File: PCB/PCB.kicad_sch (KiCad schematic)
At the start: 21 parts, among them J1 Conn_02x16_Row_Letter_Last_Sh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, U1 DRV8833PWP, U2 INA219AxDCN, U3 TPS22917DBV, U4 TPS22917DBV, U6 BQ24074RGT

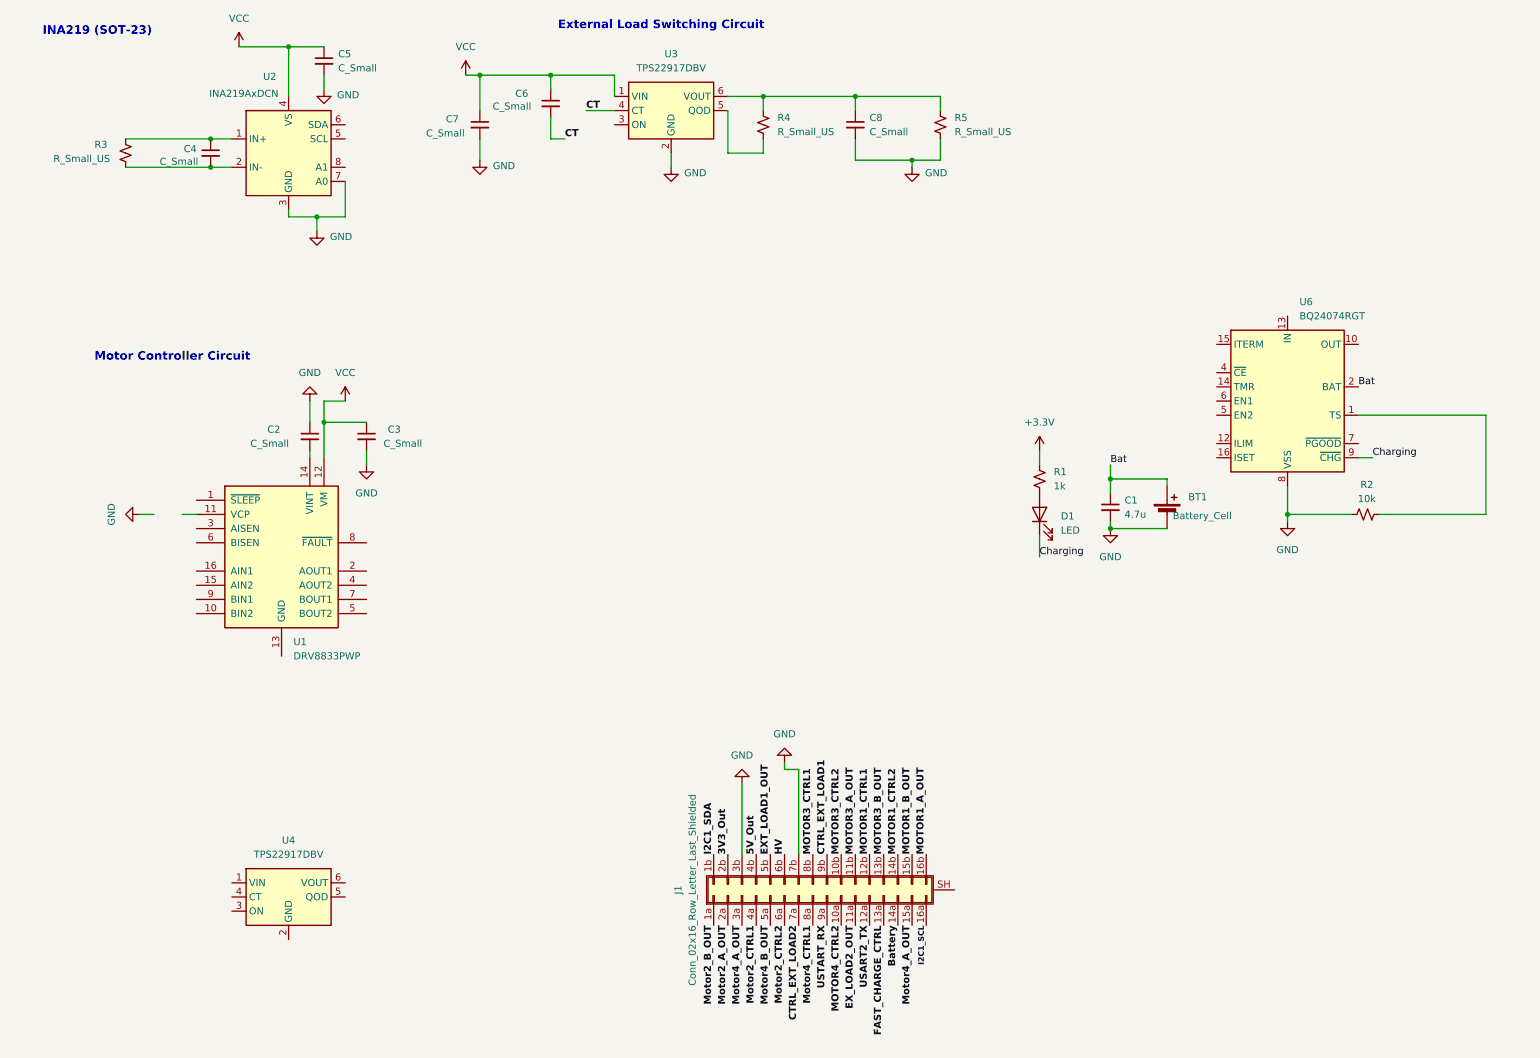
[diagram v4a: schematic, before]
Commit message: Changes to Layout
- An additional sheet was added
- ptxnya001's modules were placed into demarcated areas on her sheet
- ptxnya001's modules were given brief descriptions
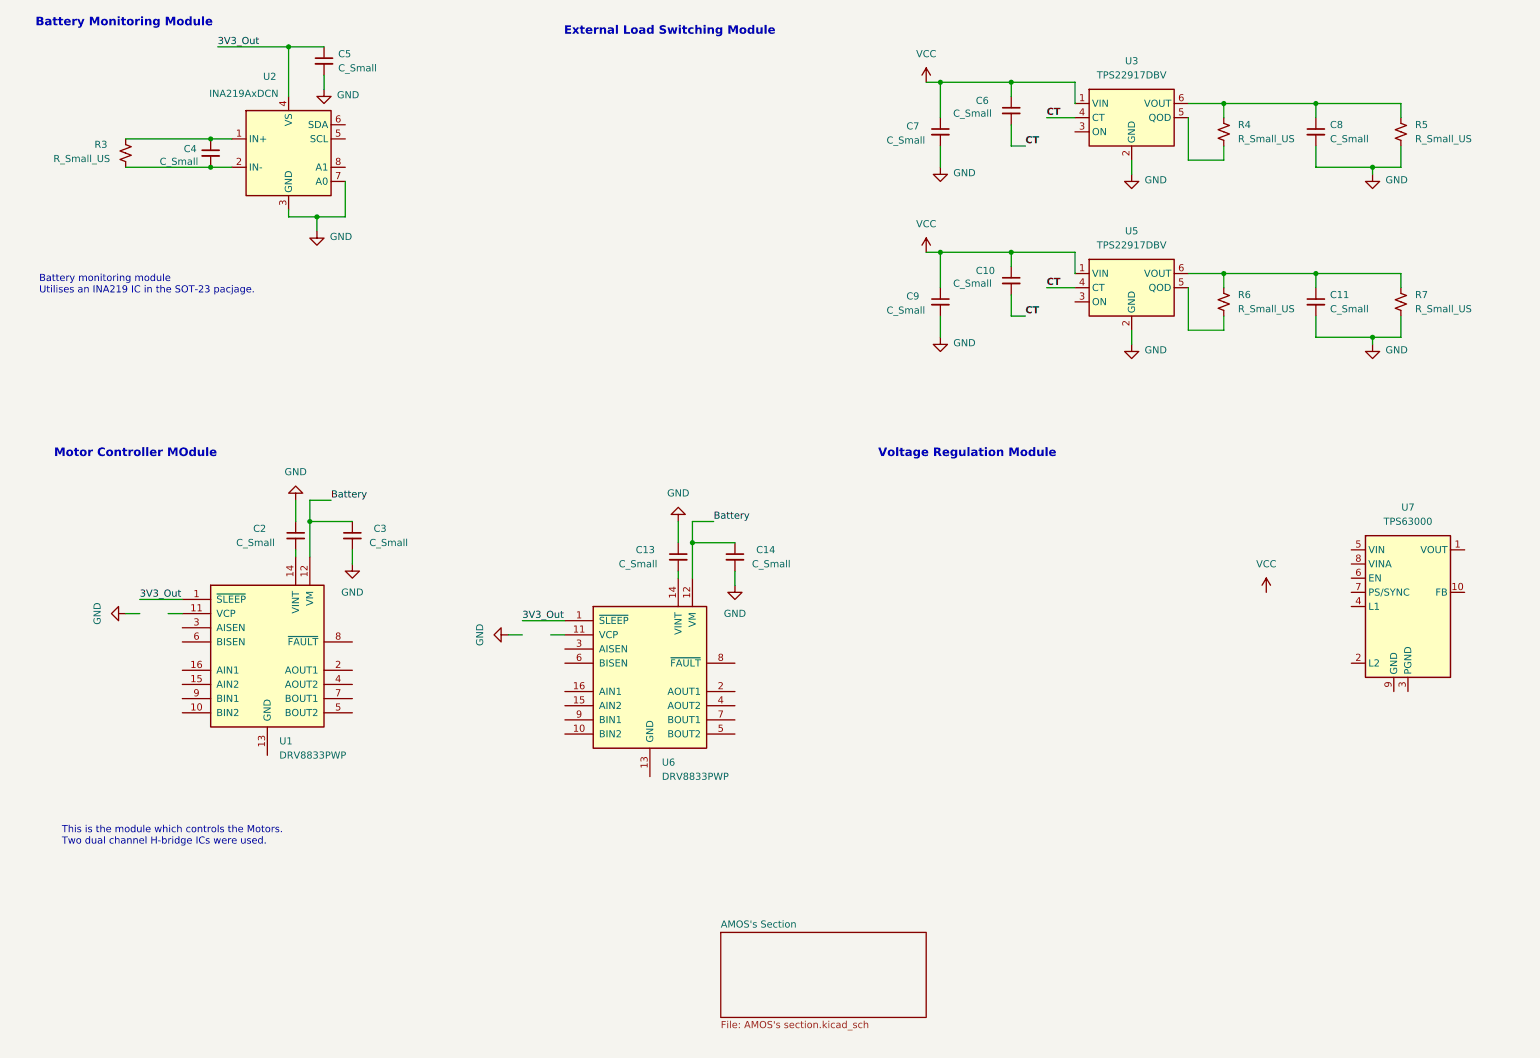
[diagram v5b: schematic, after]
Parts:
- removed BT1: Battery_Cell, symbol Device:Battery_Cell
- removed C1: 4.7u, symbol Device:C_Small
- removed D1: LED, symbol Device:LED
- removed J1: Conn_02x16_Row_Letter_Last_Shielded, symbol Connector_Generic_Shielded:Conn_02x16_Row_Letter_Last_Shielded
- removed R1: 1k, symbol Device:R_Small_US
- removed R2: 10k, symbol Device:R_Small_US
- removed U4: TPS22917DBV, Package_TO_SOT_SMD:SOT-23-6, symbol Power_Management:TPS22917DBV
- removed U6: BQ24074RGT, Package_DFN_QFN:VQFN-16-1EP_3x3mm_P0.5mm_EP1.6x1.6mm, symbol Battery_Management:BQ24074RGT
- added C10, C11, C13, C14, C9: C_Small, symbol Device:C_Small
- added R6, R7: R_Small_US, symbol Device:R_Small_US
- added U5: TPS22917DBV, Package_TO_SOT_SMD:SOT-23-6, symbol Power_Management:TPS22917DBV
- added U6: DRV8833PWP, Package_SO:HTSSOP-16-1EP_4.4x5mm_P0.65mm_EP3.4x5mm_Mask2.46x2.31mm_ThermalVias, symbol Driver_Motor:DRV8833PWP
- added U7: TPS63000, Package_SON:Texas_DRC0010J_ThermalVias, symbol Regulator_Switching:TPS63000
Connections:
- net 3V3_Out: now also C5.1, U1.1 (~{SLEEP}), U2.4 (VS), U6.1 (~{SLEEP})
- net Battery: now also C3.1, U1.12 (VM), C14.1, U6.12 (VM)
- net CT: now also C10.2, U5.4 (CT)
- net GND: now also C11.2, C13.1, C14.2, C9.2, R7.2, U5.2 (GND)
- net VCC: now also C10.1, C9.1, U5.1 (VIN); no longer C3.1, C5.1, U1.12 (VM), U2.4 (VS)
- new net: R6.2, U5.5 (QOD)
- new net: C11.1, R6.1, R7.1, U5.6 (VOUT)
- new net: U6.13 (GND), U6.17 (GND)
- new net: C13.2, U6.14 (VINT)
- new net: U7.11 (PGND), U7.3 (PGND)
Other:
- added sheet AMOS's Section (AMOS's section.kicad_sch)
- note added: "Battery Monitoring Module"
- note added: "Battery monitoring module Utilises an INA219 IC in the SOT-23 pacjage."
- note added: "External Load Switching Module"
- note added: "Motor Controller MOdule"
- note added: "This is the module which controls the Motors. Two dual channel H-bridge ICs were used."
- note added: "Voltage Regulation Module"
- note removed: "External Load Switching Circuit"
- note removed: "INA219 (SOT-23)"
- note removed: "Motor Controller Circuit"
- moved on the sheet: C2, C3, C6, C7, C8, R4, R5, U1, U3

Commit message: Updated Voltage regulator circuit
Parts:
- removed U6: DRV8833PWP, Package_SO:HTSSOP-16-1EP_4.4x5mm_P0.65mm_EP3.4x5mm_Mask2.46x2.31mm_ThermalVias, symbol Driver_Motor:DRV8833PWP
- removed U7: TPS63000, Package_SON:Texas_DRC0010J_ThermalVias, symbol Regulator_Switching:TPS63000
- added U10, U9: TPS63020, Package_DFN_QFN:Texas_S-PWQFN-N16_EP1.2x0.8mm_ThermalVias, symbol Converter_DCDC:TPS43060RTE
- added U4: DRV8833PWP, Package_SO:HTSSOP-16-1EP_4.4x5mm_P0.65mm_EP3.4x5mm_Mask2.46x2.31mm_ThermalVias, symbol Driver_Motor:DRV8833PWP
- U1: LCSC (none) -> C50506
- U2: LCSC (none) -> C87469
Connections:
- net 3V3_Out: now also U4.1 (~{SLEEP})
- net GND: now also U1.13 (GND), U1.17 (GND), U4.13 (GND), U4.17 (GND)
- net VCC: no longer C6.1, C7.1, U3.1 (VIN)
- net at C13.2: now also U4.14 (VINT)
- net Switch: now reaches C4.1, R3.1, U2.1 (IN+)
- net Battery_OUT: now reaches C4.2, R3.2, U2.2 (IN-)
- net Battery_OUT: now also C3.1, C6.1, C7.1, U1.11 (VCP), U1.12 (VM), U3.1 (VIN), U10.10 (VIN2), U10.11 (VIN1)
- net PD13/TIM4C2: now reaches U1.10 (BIN2)
- net PD13/TIM4C2: now also U4.10 (BIN2)
- net PC9/TIM3C4: now reaches U1.15 (AIN2)
- net PC9/TIM3C4: now also U4.15 (AIN2)
- net PC8/TIM3C3: now reaches U1.16 (AIN1)
- net PC8/TIM3C3: now also U4.16 (AIN1)
- net MOTOR1_A_OUT: now reaches U1.2 (AOUT1)
- net MOTOR1_A_OUT: now also U1.5 (BOUT2), U4.2 (AOUT1), U4.5 (BOUT2)
- net MOTOR2_A_OUT: now reaches U1.4 (AOUT2)
- net MOTOR2_A_OUT: now also U4.4 (AOUT2)
- net MOTOR1_B_OUT: now reaches U1.7 (BOUT1)
- net MOTOR1_B_OUT: now also U4.7 (BOUT1)
- net PD12/TIM4C1: now reaches U1.9 (BIN1)
- net PD12/TIM4C1: now also U4.9 (BIN1)
- net PB8: now reaches U2.5 (SCL)
- net PB9: now reaches U2.6 (SDA)
- net 3.3V_Out: now reaches U2.8 (A1)
- removed net Battery: C14.1, C3.1, U1.12 (VM)
- new net: U10. (PGND), U10.17 (AGND)
- new net: U9. (PGND), U9.17 (AGND)
- new net 5.5V_OUT: U10.5 (VOUT2)
- new net 5.5V_REG: U10.4 (VOUT1), U9.11 (VIN1)
- new net VM: C14.1, U4.11 (VCP), U4.12 (VM)
- no-connect marks 0 -> 2
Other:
- moved on the sheet: C2, C3, U1

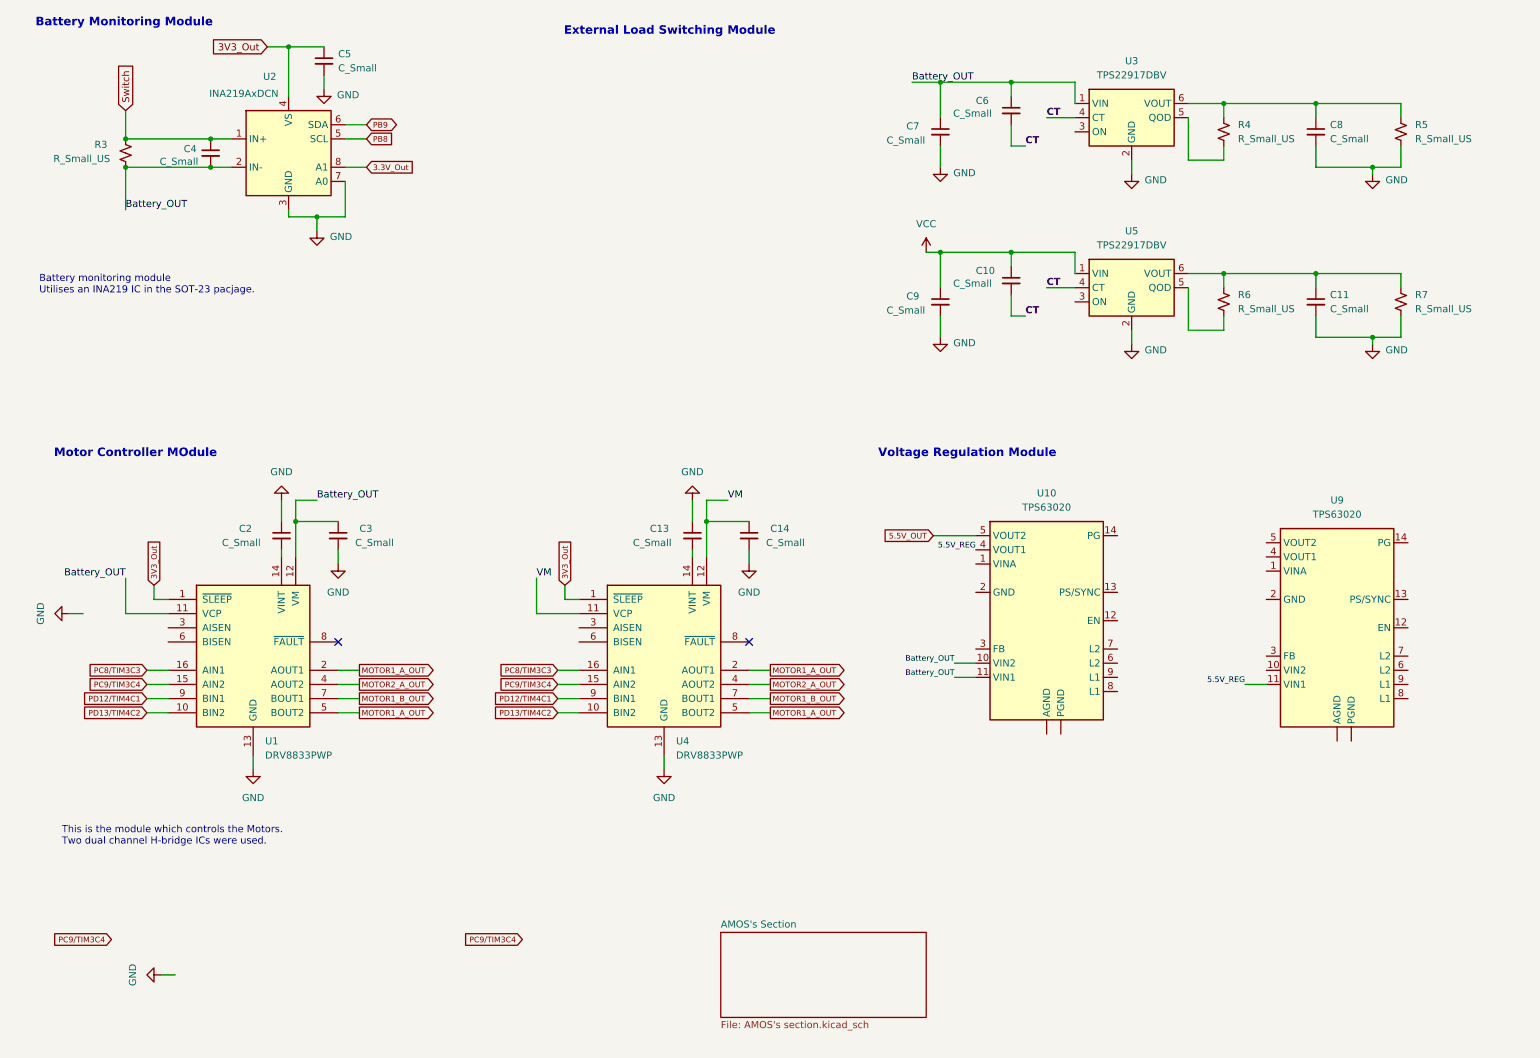
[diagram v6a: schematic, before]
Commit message: IC footprints and H-bridge test points
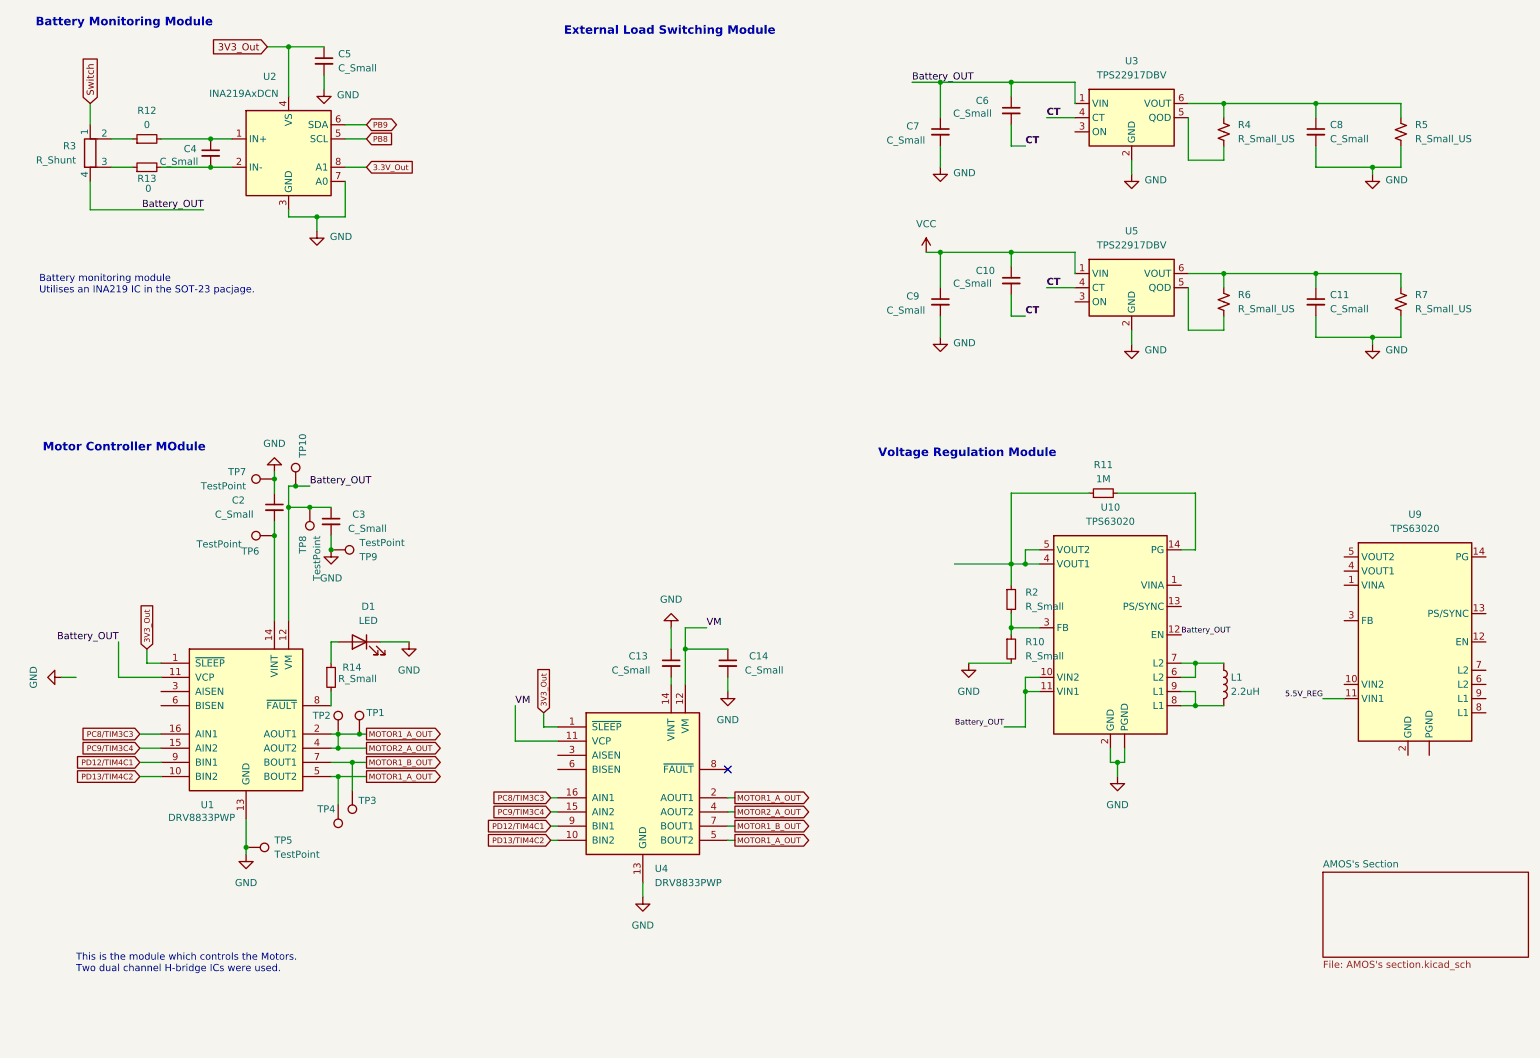
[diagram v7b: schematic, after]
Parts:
- removed R3: R_Small_US, symbol Device:R_Small_US
- added D1: LED, symbol Device:LED
- added L1: 2.2uH, symbol Device:L
- added R10, R14, R2: R_Small, symbol Device:R_Small
- added R11: 1M, symbol Device:R_Small
- added R12, R13: 0, symbol Device:R_Small
- added R3: R_Shunt, symbol Device:R_Shunt
- added TP1, TP10, TP2, TP3, TP4, TP5, TP6, TP7, TP8, TP9: TestPoint, symbol Connector:TestPoint
- U10: LCSC (none) -> C15483
- U2: footprint Package_TO_SOT_SMD:SOT-23-8 -> Library:INA219AIDCNR
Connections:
- net MOTOR2_A_OUT is gone; now on net MOTOR1_A_OUT: U1.4 (AOUT2), U4.4 (AOUT2)
- net 5.5V_REG: no longer U10.4 (VOUT1)
- net Battery_OUT: now also U10.12 (EN), R3.4, TP10.1, TP8.1; no longer C4.2, U2.2 (IN-)
- net GND: now also U10. (PGND), U10.17 (AGND), U10.2 (GND), D1.1 (K), R10.2, TP5.1, TP7.1, TP9.1
- net MOTOR1_A_OUT: now also TP1.1, TP2.1, TP4.1
- net MOTOR1_B_OUT: now also TP3.1
- net Switch: now also R3.1; no longer C4.1, U2.1 (IN+)
- net at U10.14 (PG): now also R11.2
- net at U10.3 (FB): now also R10.1, R2.2
- net at U10.6 (L2): now also U10.7 (L2), L1.1
- net at U10.8 (L1): now also U10.9 (L1), L1.2
- net at C2.2, U1.14 (VINT): now also TP6.1
- net at U1.8 (~{FAULT}): now also R14.2
- net at U9.17 (AGND): no longer U9. (PGND)
- net 5.5V_OUT: no longer names the net of U10.5 (VOUT2)
- net 5.5V_OUT: now also U10.4 (VOUT1), R11.1, R2.1
- new net: R12.1, R3.2
- new net: C4.1, R12.2, U2.1 (IN+)
- new net: R13.1, R3.3
- new net: C4.2, R13.2, U2.2 (IN-)
- new net: D1.2 (A), R14.1
- no-connect marks 2 -> 1
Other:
- moved on the sheet: C13, C14, C2, C3, U1, U4
